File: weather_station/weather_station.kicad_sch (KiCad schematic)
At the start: 22 parts, among them J1 Conn_02x03_Odd_Even, U1 ESP32-WROOM-32, U2 BME280, U3 LM2594HVN-3.3

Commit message: Initial KiCAD schematic
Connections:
- net +3.3V: now also C6.1, L1.2, U3.4 (FB)
- net GND: now also D1.1 (K), D2.1 (K), D3.1 (K), D4.1 (K)
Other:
- moved on the sheet: C3, C4, D1, D2, D3, D4, R1, R2, R3, R4, U1

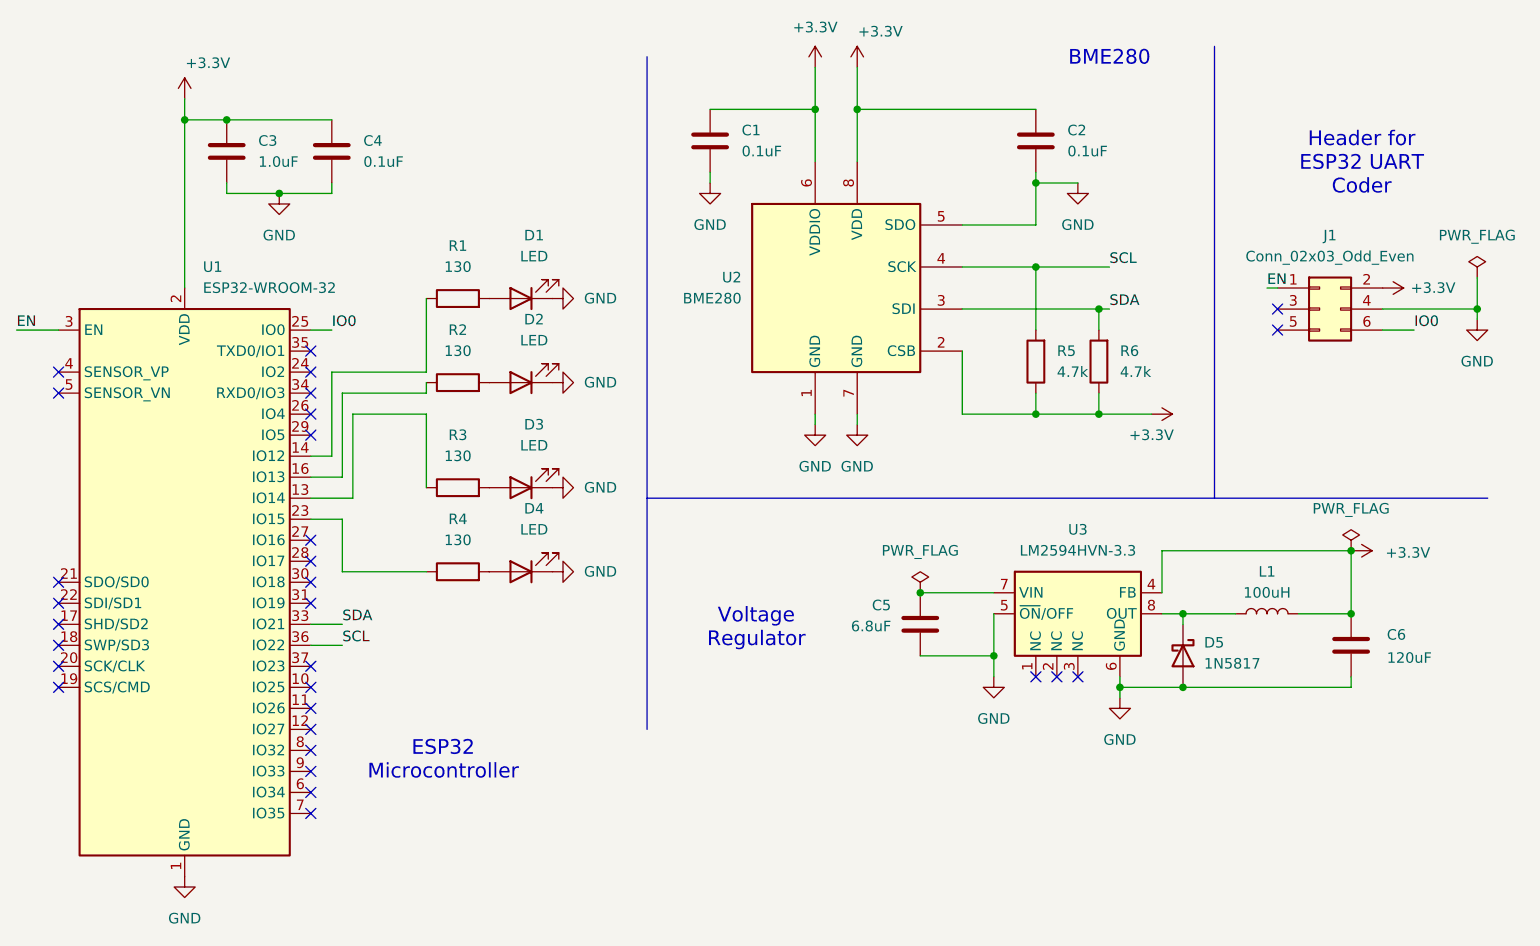
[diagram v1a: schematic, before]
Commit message: Added XT60 battery connector
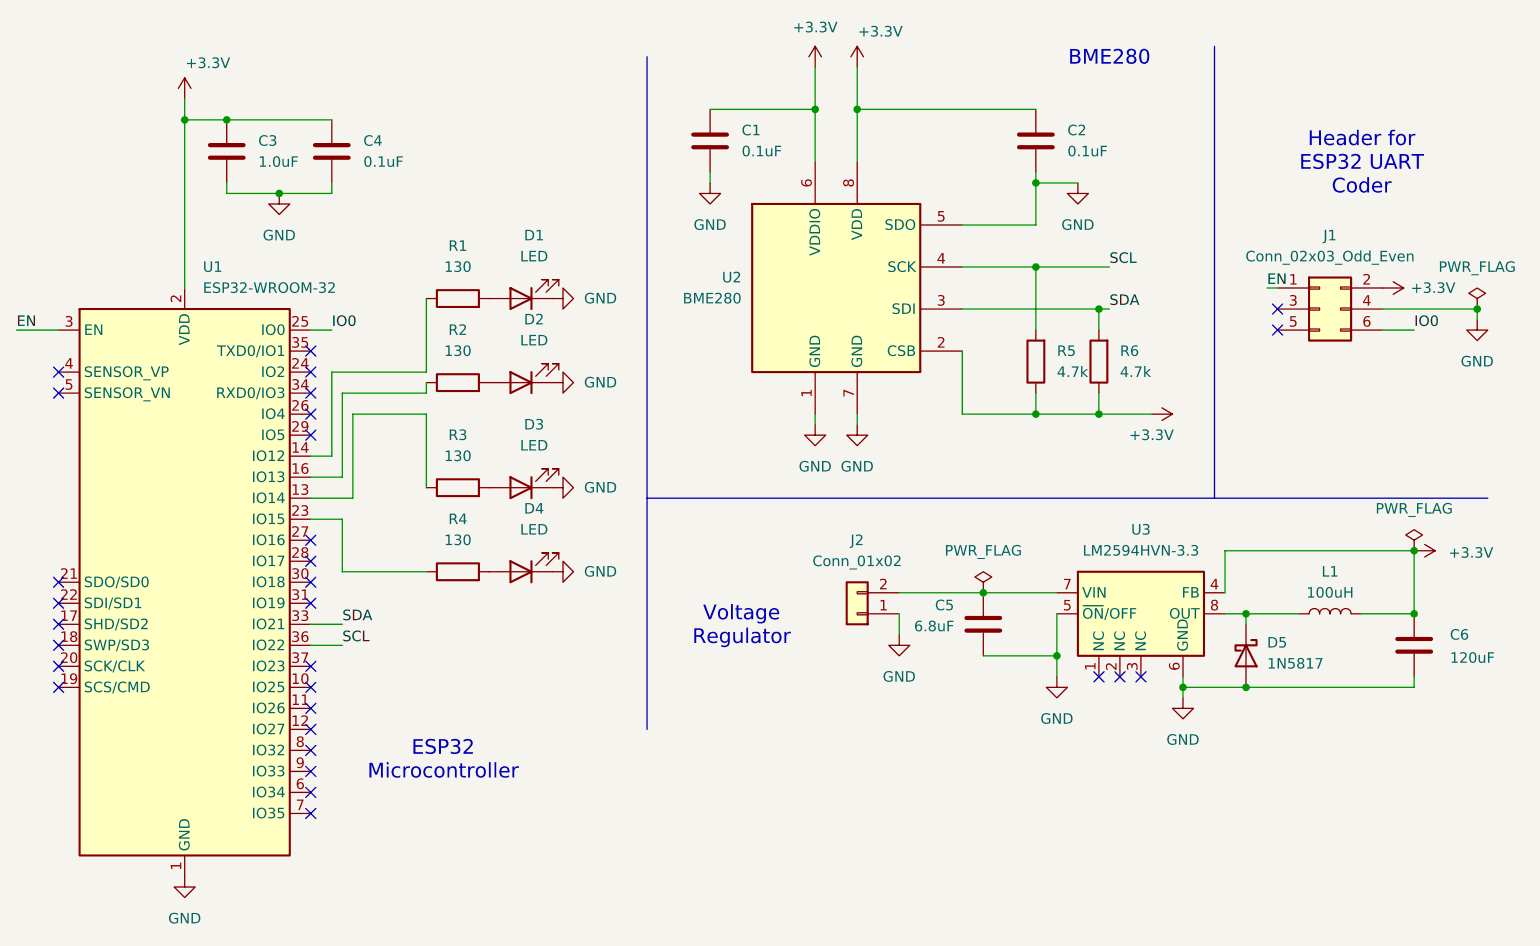
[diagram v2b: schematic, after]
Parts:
- added J2: Conn_01x02, Connector_AMASS:AMASS_XT60-F_1x02_P7.20mm_Vertical, symbol Connector_Generic:Conn_01x02
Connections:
- net GND: now also J2.1 (Pin_1)
- net at C5.1, U3.7 (VIN): now also J2.2 (Pin_2)
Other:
- moved on the sheet: C5, C6, D5, L1, U3

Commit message: Assigned footprints
Assigned footprints to LEDs, resistors, capacitors, and inductor.
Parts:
- C1, C2, C3, C4: footprint (none) -> Capacitor_THT:CP_Radial_D10.0mm_P5.00mm
- C5: footprint (none) -> Capacitor_THT:CP_Radial_D5.0mm_P2.50mm
- C6: footprint (none) -> Capacitor_THT:CP_Radial_D5.0mm_P2.00mm
- D1, D2, D3, D4: footprint (none) -> LED_THT:LED_D3.0mm
- L1: footprint (none) -> Inductor_THT:L_Axial_L5.3mm_D2.2mm_P2.54mm_Vertical_Vishay_IM-1
- R1, R2, R3, R4, R5, R6: footprint (none) -> Resistor_THT:R_Axial_DIN0204_L3.6mm_D1.6mm_P1.90mm_Vertical
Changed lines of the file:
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@@
 			)
 		)
-		(property "Footprint" ""
+		(property "Footprint" "Resistor_THT:R_Axial_DIN0204_L3.6mm_D1.6mm_P1.90mm_Vertical"
 			(at 147.828 55.88 90)
 			(effects
@@
 			)
 		)
-		(property "Footprint" ""
+		(property "Footprint" "Capacitor_THT:CP_Radial_D10.0mm_P5.00mm"
 			(at 54.3052 34.29 0)
 			(effects
@@
 			)
 		)
-		(property "Footprint" ""
+		(property "Footprint" "LED_THT:LED_D3.0mm"
 			(at 76.2 48.26 0)
 			(effects
@@
 			)
 		)
-		(property "Footprint" ""
+		(property "Footprint" "Resistor_THT:R_Axial_DIN0204_L3.6mm_D1.6mm_P1.90mm_Vertical"
 			(at 68.58 83.058 90)
 			(effects
@@
 			)
 		)
-		(property "Footprint" ""
+		(property "Footprint" "Capacitor_THT:CP_Radial_D10.0mm_P5.00mm"
 			(at 41.6052 34.29 0)
 			(effects
@@
 			)
 		)
-		(property "Footprint" ""
+		(property "Footprint" "LED_THT:LED_D3.0mm"
 			(at 76.2 71.12 0)
 			(effects
@@
 			)
 		)
-		(property "Footprint" ""
+		(property "Footprint" "LED_THT:LED_D3.0mm"
 			(at 76.2 58.42 0)
 			(effects
@@
 			)
 		)
-		(property "Footprint" ""
+		(property "Footprint" "Capacitor_THT:CP_Radial_D5.0mm_P2.50mm"
 			(at 133.0452 91.44 0)
 			(effects
@@
 			)
 		)
-		(property "Footprint" ""
+		(property "Footprint" "Resistor_THT:R_Axial_DIN0204_L3.6mm_D1.6mm_P1.90mm_Vertical"
 			(at 140.208 55.88 90)
 			(effects
@@
 			)
 		)
-		(property "Footprint" ""
+		(property "Footprint" "Capacitor_THT:CP_Radial_D10.0mm_P5.00mm"
 			(at 100.0252 33.02 0)
 			(effects
@@
 			)
 		)
-		(property "Footprint" ""
+		(property "Footprint" "Capacitor_THT:CP_Radial_D10.0mm_P5.00mm"
 			(at 139.3952 33.02 0)
 			(effects
@@
 			)
 		)
-		(property "Footprint" ""
+		(property "Footprint" "Resistor_THT:R_Axial_DIN0204_L3.6mm_D1.6mm_P1.90mm_Vertical"
 			(at 68.58 60.198 90)
 			(effects
@@
 			)
 		)
-		(property "Footprint" ""
+		(property "Footprint" "Capacitor_THT:CP_Radial_D5.0mm_P2.00mm"
 			(at 185.1152 93.98 0)
 			(effects
@@
 			)
 		)
-		(property "Footprint" ""
+		(property "Footprint" "Inductor_THT:L_Axial_L5.3mm_D2.2mm_P2.54mm_Vertical_Vishay_IM-1"
 			(at 173.99 86.36 0)
 			(effects
@@
 			)
 		)
-		(property "Footprint" ""
+		(property "Footprint" "Resistor_THT:R_Axial_DIN0204_L3.6mm_D1.6mm_P1.90mm_Vertical"
 			(at 68.58 72.898 90)
 			(effects
@@
 			)
 		)
-		(property "Footprint" ""
+		(property "Footprint" "Resistor_THT:R_Axial_DIN0204_L3.6mm_D1.6mm_P1.90mm_Vertical"
 			(at 68.58 50.038 90)
 			(effects
@@
 			)
 		)
-		(property "Footprint" ""
+		(property "Footprint" "LED_THT:LED_D3.0mm"
 			(at 76.2 81.28 0)
 			(effects
